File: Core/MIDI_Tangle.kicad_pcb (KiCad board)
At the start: 2 copper layers, 40 x 97.5 mm, 97 parts, among them J1 USB_C_Receptacle_USB2.0, J2 Conn_01x04, J21 Conn_02x08_Odd_Even, J4 Conn_01x06_Male, J5 Conn_01x08_Female, J6 Conn_01x08_Female, J7 Conn_01x08_Female, J8 Conn_01x08_Female, Q1 BSS84, Q2 2N7002, Q3 BSS84, SW1 SW_Push_DPDT, SW2 SW_SPST, SW3 SW_SPST, U1 ATSAMD21G15B-A, U10 TL072, U11 TL072, U12 TL072, U13 TL072, U14 MCP2517FD-xSL, U15 TLE9250V, U16 CAT250xxx, U17 74HC595, U18 MIC5504-3.3YM5, U19 74HC595, U2 DG408, U20 74HC595, U3 DG408, U4 DG408, U5 DG408, U6 DG408, U7 DG408, U8 DG408, U9 DG408, Y1 20MHz

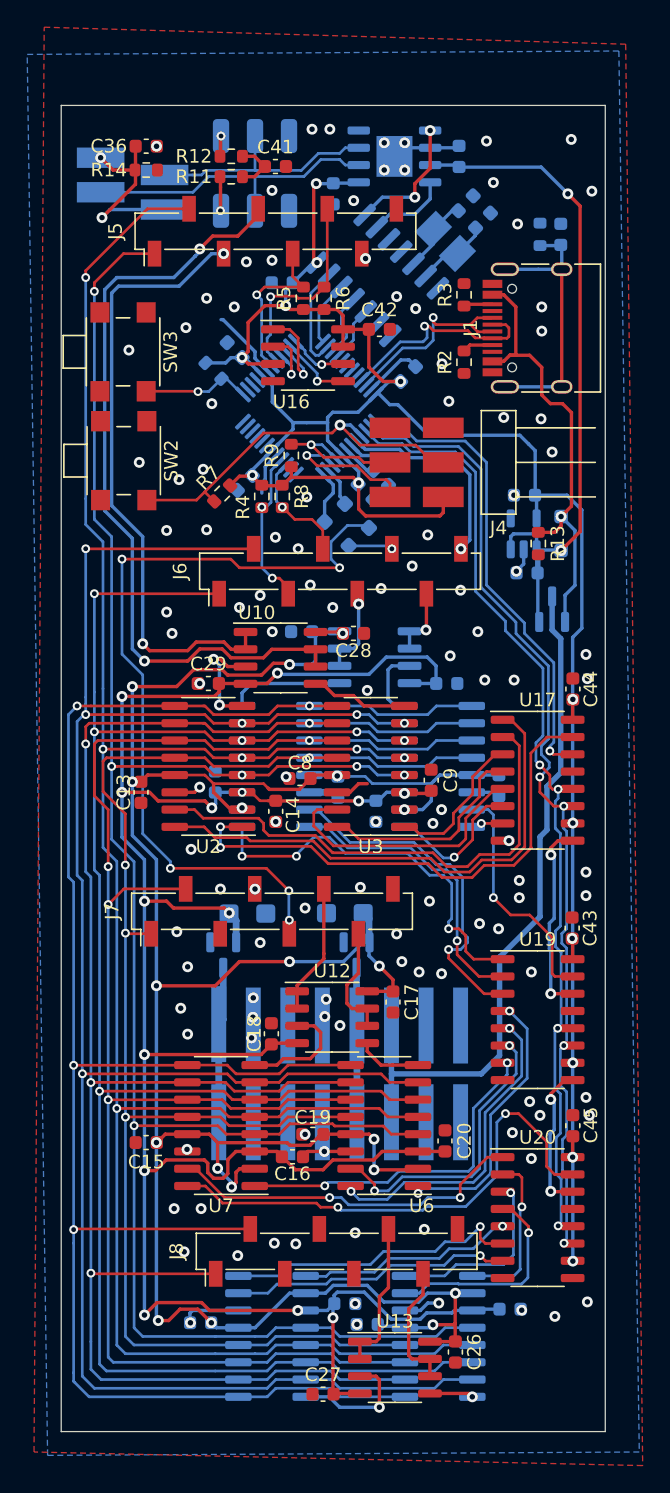
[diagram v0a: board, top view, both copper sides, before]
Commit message: Reduce output capacitive load
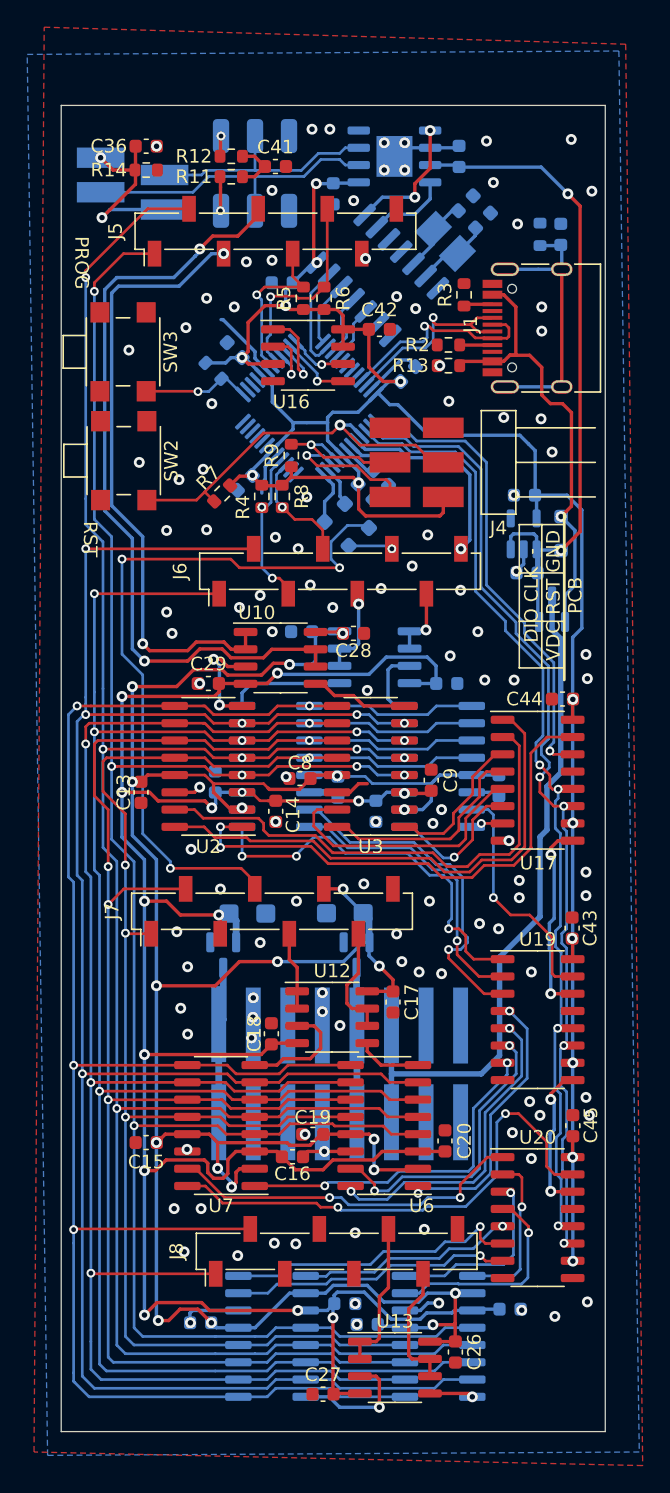
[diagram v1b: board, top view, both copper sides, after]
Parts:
- moved R13 14.7 mm to (188.7, 71.9), turned to 180 degrees
- moved R2 1.71 mm to (188.7, 70.4), turned to 0 degrees
- moved C44 1.06 mm to (197.1, 96.4), turned to 180 degrees
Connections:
- J7 pad 3: GND -> -VDC
- J7 pad 4: GND -> Butt_Y
- J7 pad 5: Butt_Y -> Out6
- J7 pad 6: Out6 -> +VDC
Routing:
- net Butt_Y: track 58.5 -> 53.1 mm, vias 5 -> 3
- net Out6: track 9.61 -> 5.74 mm
- net +VDC: track 198.3 -> 202.1 mm, vias 19 -> 20
- net -VDC: track 183.4 -> 184.9 mm
- net GND: vias 119 -> 118
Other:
- board text added: "DIO CLK - VDC RST GND PCB"
- board text added: "PROG"
- board text added: "RST"

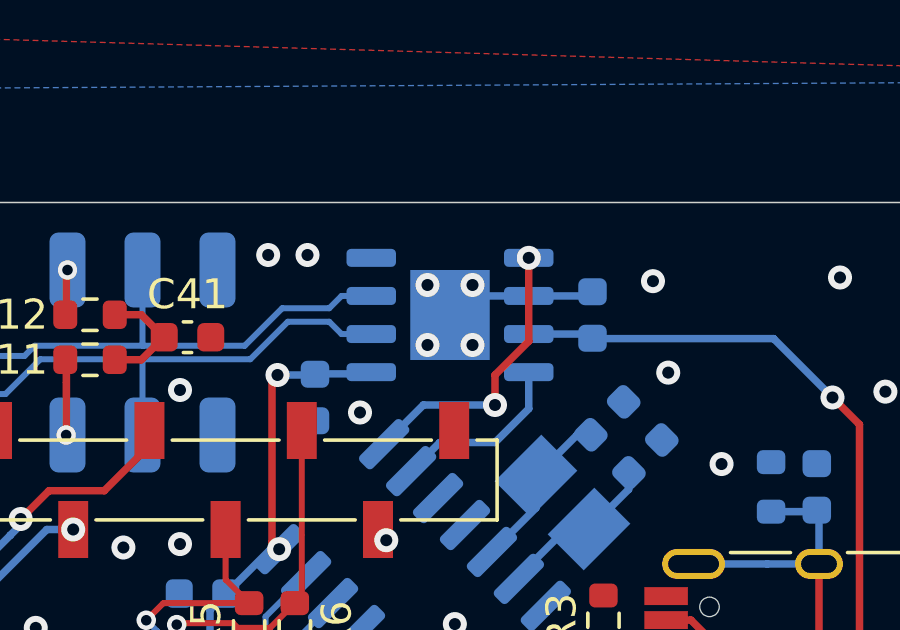
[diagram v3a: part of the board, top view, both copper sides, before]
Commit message: Change CAN tranceiver to MCP2562
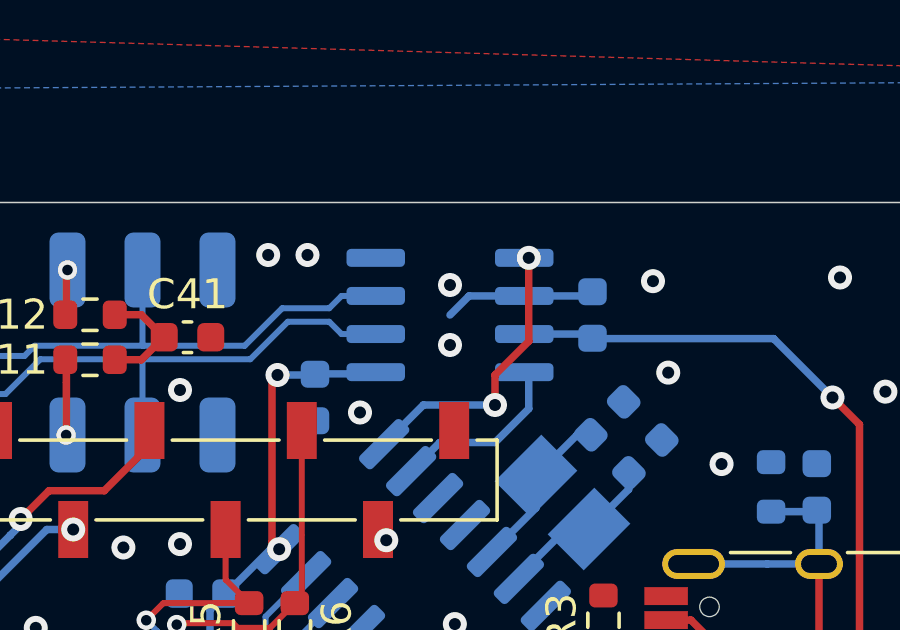
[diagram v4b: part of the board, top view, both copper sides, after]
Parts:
- U15: value TLE9250V -> MCP2562FD-ESN; footprint Package_SO:Infineon_PG-DSO-8-27_3.9x4.9mm_EP2.65x3mm -> Package_SO:SOIC-8_3.9x4.9mm_P1.27mm
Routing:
- net GND: vias 118 -> 116
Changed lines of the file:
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@@
     )
   )
-  (footprint "Package_SO:Infineon_PG-DSO-8-27_3.9x4.9mm_EP2.65x3mm" (layer "B.Cu")
+  (footprint "Package_SO:SOIC-8_3.9x4.9mm_P1.27mm" (layer "B.Cu")
     (at 184.75 56.5 180)
-    (descr "Infineon  PG-DSO, 8 Pin (https://www.infineon.com/cms/en/product/packages/PG-DSO/PG-DSO-8-27), generated with kicad-footprint-generator ipc_gullwing_generator.py")
-    (tags "Infineon PG-DSO SO")
+    (descr "SOIC, 8 Pin (JEDEC MS-012AA, https://www.analog.com/media/en/package-pcb-resources/package/pkg_pdf/soic_narrow-r/r_8.pdf), generated with kicad-footprint-generator ipc_gullwing_generator.py")
+    (tags "SOIC SO")
     (property "Sheetfile" "MIDI_Tangle.kicad_sch")
     (property "Sheetname" "")
-    (property "ki_description" "CAN FD Transceiver with Silent Mode, up to 8 Mbps, DFN-8")
-    (property "ki_keywords" "CAN FD Transceiver")
+    (property "ki_description" "High-Speed CAN Transceiver, 1Mbps, 5V supply, Vio pin, -40C to +125C, SOIC-8")
+    (property "ki_keywords" "High-Speed CAN Transceiver")
     (attr smd)
     (fp_text reference "U15" (at -5.25 2.5) (layer "B.SilkS")
         (effects (font (size 1 1) (thickness 0.15)) (justify mirror))
     )
-    (fp_text value "TLE9250V" (at 0 -3.4) (layer "B.Fab")
+    (fp_text value "MCP2562FD-ESN" (at 0 -3.4) (layer "B.Fab")
         (effects (font (size 1 1) (thickness 0.15)) (justify mirror))
     )
@@
     (fp_line (start 1.95 2.45) (end 1.95 -2.45)
       (stroke (width 0.1) (type solid)) (layer "B.Fab"))
-    (pad "" smd roundrect (at -0.66 -0.75 180) (size 1.07 1.21) (layers "B.Paste") (roundrect_rratio 0.233645))
-    (pad "" smd roundrect (at -0.66 0.75 180) (size 1.07 1.21) (layers "B.Paste") (roundrect_rratio 0.233645))
-    (pad "" smd roundrect (at 0.66 -0.75 180) (size 1.07 1.21) (layers "B.Paste") (roundrect_rratio 0.233645))
-    (pad "" smd roundrect (at 0.66 0.75 180) (size 1.07 1.21) (layers "B.Paste") (roundrect_rratio 0.233645))
-    (pad "1" smd roundrect (at -2.625 1.905 180) (size 1.65 0.6) (layers "B.Cu" "B.Paste" "B.Mask") (roundrect_rratio 0.25)
+    (pad "1" smd roundrect (at -2.475 1.905 180) (size 1.95 0.6) (layers "B.Cu" "B.Paste" "B.Mask") (roundrect_rratio 0.25)
       (net 125 "Net-(U14-TXCAN)") (pinfunction "TXD") (pintype "input"))
-    (pad "2" smd roundrect (at -2.625 0.635 180) (size 1.65 0.6) (layers "B.Cu" "B.Paste" "B.Mask") (roundrect_rratio 0.25)
+    (pad "2" smd roundrect (at -2.475 0.635 180) (size 1.95 0.6) (layers "B.Cu" "B.Paste" "B.Mask") (roundrect_rratio 0.25)
       (net 1 "GND") (pinfunction "VSS") (pintype "power_in"))
-    (pad "3" smd roundrect (at -2.625 -0.635 180) (size 1.65 0.6) (layers "B.Cu" "B.Paste" "B.Mask") (roundrect_rratio 0.25)
+    (pad "3" smd roundrect (at -2.475 -0.635 180) (size 1.95 0.6) (layers "B.Cu" "B.Paste" "B.Mask") (roundrect_rratio 0.25)
       (net 9 "+5V") (pinfunction "VDD") (pintype "power_in"))
-    (pad "4" smd roundrect (at -2.625 -1.905 180) (size 1.65 0.6) (layers "B.Cu" "B.Paste" "B.Mask") (roundrect_rratio 0.25)
+    (pad "4" smd roundrect (at -2.475 -1.905 180) (size 1.95 0.6) (layers "B.Cu" "B.Paste" "B.Mask") (roundrect_rratio 0.25)
       (net 124 "Net-(U14-RXCAN)") (pinfunction "RXD") (pintype "output"))
-    (pad "5" smd roundrect (at 2.625 -1.905 180) (size 1.65 0.6) (layers "B.Cu" "B.Paste" "B.Mask") (roundrect_rratio 0.25)
-      (net 6 "+3V3") (pinfunction "VIO") (pintype "power_in"))
-    (pad "6" smd roundrect (at 2.625 -0.635 180) (size 1.65 0.6) (layers "B.Cu" "B.Paste" "B.Mask") (roundrect_rratio 0.25)
+    (pad "5" smd roundrect (at 2.475 -1.905 180) (size 1.95 0.6) (layers "B.Cu" "B.Paste" "B.Mask") (roundrect_rratio 0.25)
+      (net 6 "+3V3") (pinfunction "Vio") (pintype "power_in"))
+    (pad "6" smd roundrect (at 2.475 -0.635 180) (size 1.95 0.6) (layers "B.Cu" "B.Paste" "B.Mask") (roundrect_rratio 0.25)
       (net 85 "M2IDI-") (pinfunction "CANL") (pintype "bidirectional"))
-    (pad "7" smd roundrect (at 2.625 0.635 180) (size 1.65 0.6) (layers "B.Cu" "B.Paste" "B.Mask") (roundrect_rratio 0.25)
+    (pad "7" smd roundrect (at 2.475 0.635 180) (size 1.95 0.6) (layers "B.Cu" "B.Paste" "B.Mask") (roundrect_rratio 0.25)
       (net 84 "M2IDI+") (pinfunction "CANH") (pintype "bidirectional"))
-    (pad "8" smd roundrect (at 2.625 1.905 180) (size 1.65 0.6) (layers "B.Cu" "B.Paste" "B.Mask") (roundrect_rratio 0.25)
-      (net 1 "GND") (pinfunction "S") (pintype "input"))
-    (pad "9" smd rect (at 0 0 180) (size 2.65 3) (layers "B.Cu" "B.Mask")
-      (net 1 "GND") (pinfunction "VSS") (pintype "passive"))
-    (model "${KICAD6_3DMODEL_DIR}/Package_SO.3dshapes/Infineon_PG-DSO-8-27_3.9x4.9mm_EP2.65x3mm.wrl"
+    (pad "8" smd roundrect (at 2.475 1.905 180) (size 1.95 0.6) (layers "B.Cu" "B.Paste" "B.Mask") (roundrect_rratio 0.25)
+      (net 1 "GND") (pinfunction "STBY") (pintype "input"))
+    (model "${KICAD6_3DMODEL_DIR}/Package_SO.3dshapes/SOIC-8_3.9x4.9mm_P1.27mm.wrl"
       (offset (xyz 0 0 0))
       (scale (xyz 1 1 1))
@@
   (via (at 192.786 75.692) (size 0.8) (drill 0.4) (layers "F.Cu" "B.Cu") (free) (net 1))
   (via (at 178.562 88.011) (size 0.8) (drill 0.4) (layers "F.Cu" "B.Cu") (free) (net 1))
-  (via (at 184 57.5) (size 0.8) (drill 0.4) (layers "F.Cu" "B.Cu") (net 1))
+  (via (at 184.75 57.5) (size 0.8) (drill 0.4) (layers "F.Cu" "B.Cu") (net 1))
   (via (at 169.5 129.5) (size 0.8) (drill 0.4) (layers "F.Cu" "B.Cu") (net 1))
-  (via (at 185.5 55.5) (size 0.8) (drill 0.4) (layers "F.Cu" "B.Cu") (net 1))
   (via (at 188.849 93.218) (size 0.8) (drill 0.4) (layers "F.Cu" "B.Cu") (net 1))
   (via (at 198.8312 110.8456) (size 0.8) (drill 0.4) (layers "F.Cu" "B.Cu") (free) (net 1))
@@
   (via (at 192.024 58.42) (size 0.8) (drill 0.4) (layers "F.Cu" "B.Cu") (net 1))
   (via (at 174.879 114.3) (size 0.8) (drill 0.4) (layers "F.Cu" "B.Cu") (free) (net 1))
-  (via (at 184 55.5) (size 0.8) (drill 0.4) (layers "F.Cu" "B.Cu") (net 1))
+  (via (at 184.75 55.5) (size 0.8) (drill 0.4) (layers "F.Cu" "B.Cu") (net 1))
   (via (at 193.802 61.468) (size 0.8) (drill 0.4) (layers "F.Cu" "B.Cu") (net 1))
   (via (at 191.389 94.996) (size 0.8) (drill 0.4) (layers "F.Cu" "B.Cu") (free) (net 1))
@@
   (via (at 182.626 64.008) (size 0.8) (drill 0.4) (layers "F.Cu" "B.Cu") (net 1))
   (via (at 186.055 86.614) (size 0.8) (drill 0.4) (layers "F.Cu" "B.Cu") (net 1))
-  (via (at 185.5 57.5) (size 0.8) (drill 0.4) (layers "F.Cu" "B.Cu") (net 1))
   (via (at 187.325 111.252) (size 0.8) (drill 0.4) (layers "F.Cu" "B.Cu") (free) (net 1))
   (via (at 181.864 135.636) (size 0.8) (drill 0.4) (layers "F.Cu" "B.Cu") (free) (net 1))
